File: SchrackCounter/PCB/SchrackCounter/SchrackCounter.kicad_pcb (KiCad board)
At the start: 2 copper layers, 38 parts, among them IC1 TPS565242DRLR, J1 TYPE-C-31-M-12, SW1 SW_DPDT_x2, SW2 SW_Push, SW3 SW_Push, SW4 SW_Push, SW5 SW_Push, U1 D168K, U2 DC56-11EWA, U3 D168K, U4 DC56-11EWA, U5 D168K, U7 ESP32-S3-WROOM-2, U8 USBLC6-2SC6

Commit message: sleep, overated imo
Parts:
- added BT1: Battery, Connector_Samtec_HPM_THT:Samtec_HPM-02-01-x-S_Straight_1x02_Pitch5.08mm, F.Cu at (144.7, 87.8)
- added BZ1: Buzzer, Schrack_brd:CUI_CPT-1625-80, F.Cu at (86.0, 102.3)
- added D2: LED, LED_SMD:LED_0805_2012Metric_Pad1.15x1.40mm_HandSolder, F.Cu at (76.4, 94.6)
- added D3: LED, LED_SMD:LED_0805_2012Metric_Pad1.15x1.40mm_HandSolder, F.Cu at (76.4, 97.6)
- added D4: LED, LED_SMD:LED_0805_2012Metric_Pad1.15x1.40mm_HandSolder, F.Cu at (76.4, 100.6)
- added D5: LED, LED_SMD:LED_0805_2012Metric_Pad1.15x1.40mm_HandSolder, F.Cu at (76.4, 103.7)
- added D6: LED, LED_SMD:LED_0805_2012Metric_Pad1.15x1.40mm_HandSolder, F.Cu at (76.4, 106.7)
- added D7: LED, LED_SMD:LED_0805_2012Metric_Pad1.15x1.40mm_HandSolder, F.Cu at (76.4, 109.8)
- added D8: LED, LED_SMD:LED_0805_2012Metric_Pad1.15x1.40mm_HandSolder, F.Cu at (76.4, 112.8)
- added D9: LED, LED_SMD:LED_0805_2012Metric_Pad1.15x1.40mm_HandSolder, F.Cu at (76.4, 115.8)
- added J2: Conn_01x02_Pin, Connector_PinHeader_2.54mm:PinHeader_1x02_P2.54mm_Vertical, F.Cu at (149.5, 65.5)
- added J3: Conn_01x02_Pin, Connector_JST:JST_XH_B2B-XH-A_1x02_P2.50mm_Vertical, F.Cu at (150.7, 58.7)
- added M1: Fan_CPU_4pin, Connector:FanPinHeader_1x04_P2.54mm_Vertical, F.Cu at (149.5, 51.0)
- added R10: 10k.mcu, Resistor_SMD:R_0805_2012Metric_Pad1.20x1.40mm_HandSolder, F.Cu at (149.6, 71.8)
- added R3: 10k, Resistor_SMD:R_0805_2012Metric_Pad1.20x1.40mm_HandSolder, F.Cu at (110.0, 81.6)
- added R7: 15R, Resistor_SMD:R_0805_2012Metric_Pad1.20x1.40mm_HandSolder, F.Cu at (95.7, 103.4)
- added R8: 220R, Resistor_SMD:R_0805_2012Metric_Pad1.20x1.40mm_HandSolder, F.Cu at (95.7, 106.3)
- added R9: 220R, Resistor_SMD:R_0805_2012Metric_Pad1.20x1.40mm_HandSolder, F.Cu at (95.7, 109.3)
- added SW6: SW_Push, Button_Switch_SMD:SW_SPST_EVQPE1, F.Cu at (142.7, 70.0)
- added SW7: SW_Push, Button_Switch_SMD:SW_SPST_EVQPE1, F.Cu at (142.7, 75.0)
- added SW8: SW_Push, Button_Switch_SMD:SW_SPST_EVQPE1, F.Cu at (142.7, 80.1)
- added TP3: TestPoint, Schrack_brd:SCHRACK_LOGO_IMG, F.Cu at (187.2, 77.2)
- added U6: MAX7219, Package_SO:SOIC-24W_7.5x15.4mm_P1.27mm, F.Cu at (101.2, 82.6)
- C10: value 100nF.mcu -> 100nF.max
- C9: value 10uF.mcu -> 10uF.max
- R4, R5: value 15R -> 220R
- R6: value 10k.mcu -> 15R
- moved TP1 180.2 mm to (224.2, 82.0)
- moved J1 113.3 mm to (84.8, 118.3)
- moved R4 108.4 mm to (95.7, 94.5)
- moved R5 108.4 mm to (95.7, 97.5)
- moved D1 103.6 mm to (97.4, 117.8)
- moved C13 97.8 mm to (100.4, 94.5)
- moved U8 95.9 mm to (97.8, 113.9)
- moved U1 94.0 mm to (76.8, 49.2), turned to 0 degrees
- moved R6 93.6 mm to (95.7, 100.4)
- moved TP2 89.5 mm to (183.9, 90.6)
- moved U3 89.3 mm to (76.8, 63.3), turned to 0 degrees
- moved U5 88.8 mm to (76.8, 77.3), turned to 0 degrees
- moved R1 75.8 mm to (136.0, 109.6)
- moved R2 75.8 mm to (136.0, 112.5)
- moved U2 74.5 mm to (97.6, 50.5), turned to 0 degrees
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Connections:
- net TEST PROGRAM 1 renamed DIGIT_SELECT
- net TEST PROGRAM 2 renamed TIME_UP
- R4 pad 1: D+ IN -> GREEN_FLASH
- R4 pad 2: Net-(R4-Pad2) -> Net-(D2-A)
- R5 pad 1: D- IN -> GREEN_FLASH
- R5 pad 2: Net-(R5-Pad2) -> Net-(D4-A)
- R6 pad 1: EN -> D+ IN
- R6 pad 2: +3V3 -> Net-(R6-Pad2)
- U7 pad 13: unconnected-(U7-IO19-Pad13) -> D-
- U7 pad 14: unconnected-(U7-IO20-Pad14) -> D+
- U7 pad 18: unconnected-(U7-IO10-Pad18) -> ~{CS}
- U7 pad 19: unconnected-(U7-IO11-Pad19) -> MOSI
- U7 pad 20: unconnected-(U7-IO12-Pad20) -> CLK
- U7 pad 36: unconnected-(U7-RXD0-Pad36) -> RX
- U7 pad 37: unconnected-(U7-TXD0-Pad37) -> TX
- U8 pad 1: Net-(R4-Pad2) -> Net-(R6-Pad2)
- U8 pad 3: Net-(R5-Pad2) -> Net-(R7-Pad2)

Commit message: pcb Update
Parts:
- removed U2, U4: DC56-11EWA, Display_7Segment:DA56-11SURKWA
- added U9: CA56-12SURKWA, Display_7Segment:CA56-12SURKWA, F.Cu at (197.2, 106.7)
- moved U6 135.7 mm to (233.8, 53.5), turned to 180 degrees
- moved U5 129.1 mm to (204.7, 59.0), turned to 90 degrees
- moved U3 114.6 mm to (191.4, 59.0), turned to 90 degrees
- moved C14 112.9 mm to (52.5, 113.5)
- moved C15 112.9 mm to (52.5, 116.5)
- moved TP1 104.4 mm to (265.8, -13.8)
- moved TP2 104.4 mm to (225.4, -5.19)
- moved TP3 104.4 mm to (228.8, -18.5)
- moved U1 101.8 mm to (178.2, 59.0), turned to 90 degrees
- moved U7 101.4 mm to (99.4, 9.45)
- moved R10 98.7 mm to (61.8, 116.8)
- moved C1 74.3 mm to (81.8, 144.8)
- moved C11 74.3 mm to (64.7, 132.6)
- moved C2 74.3 mm to (87.2, 144.7)
- moved C4 74.3 mm to (87.2, 147.8)
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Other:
- board outline added: 100 x 50 mm

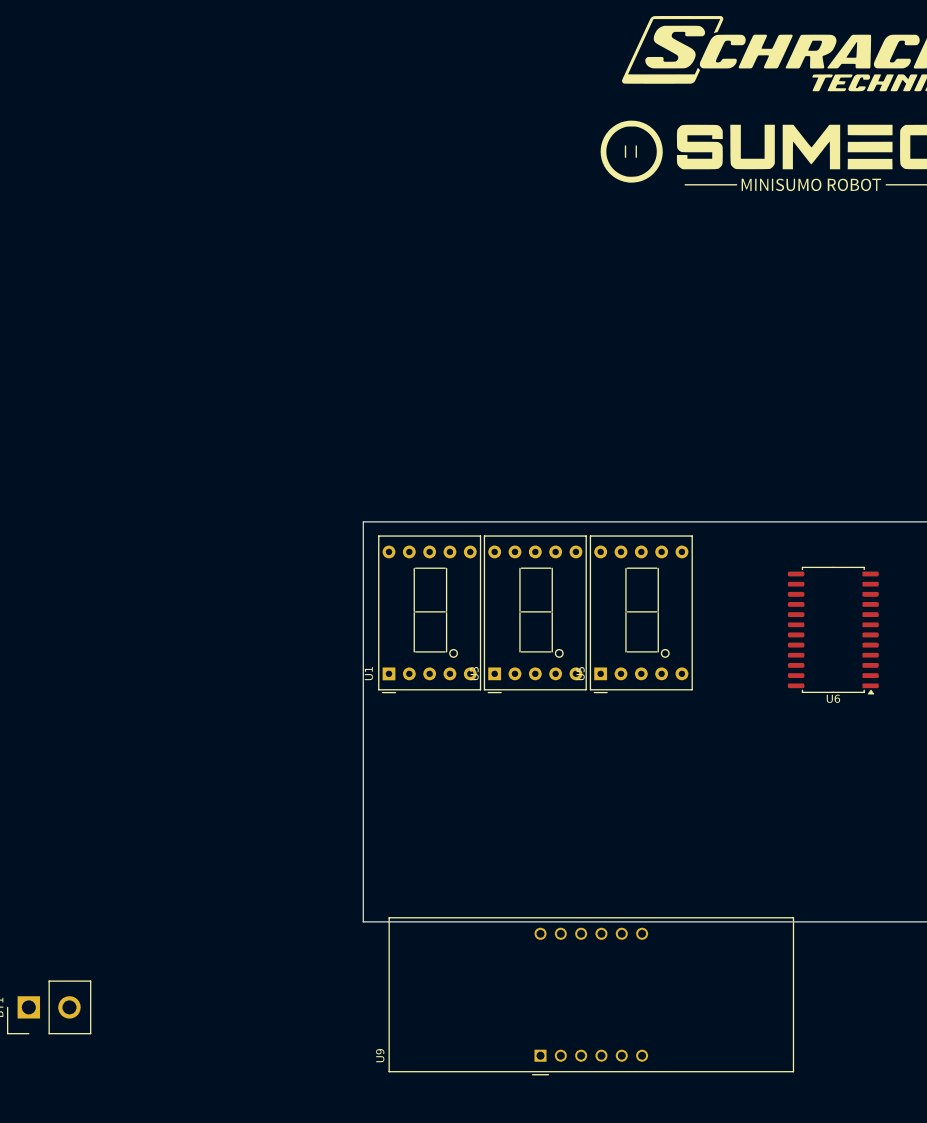
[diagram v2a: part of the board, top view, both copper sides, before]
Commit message: Custom symbol and footprints
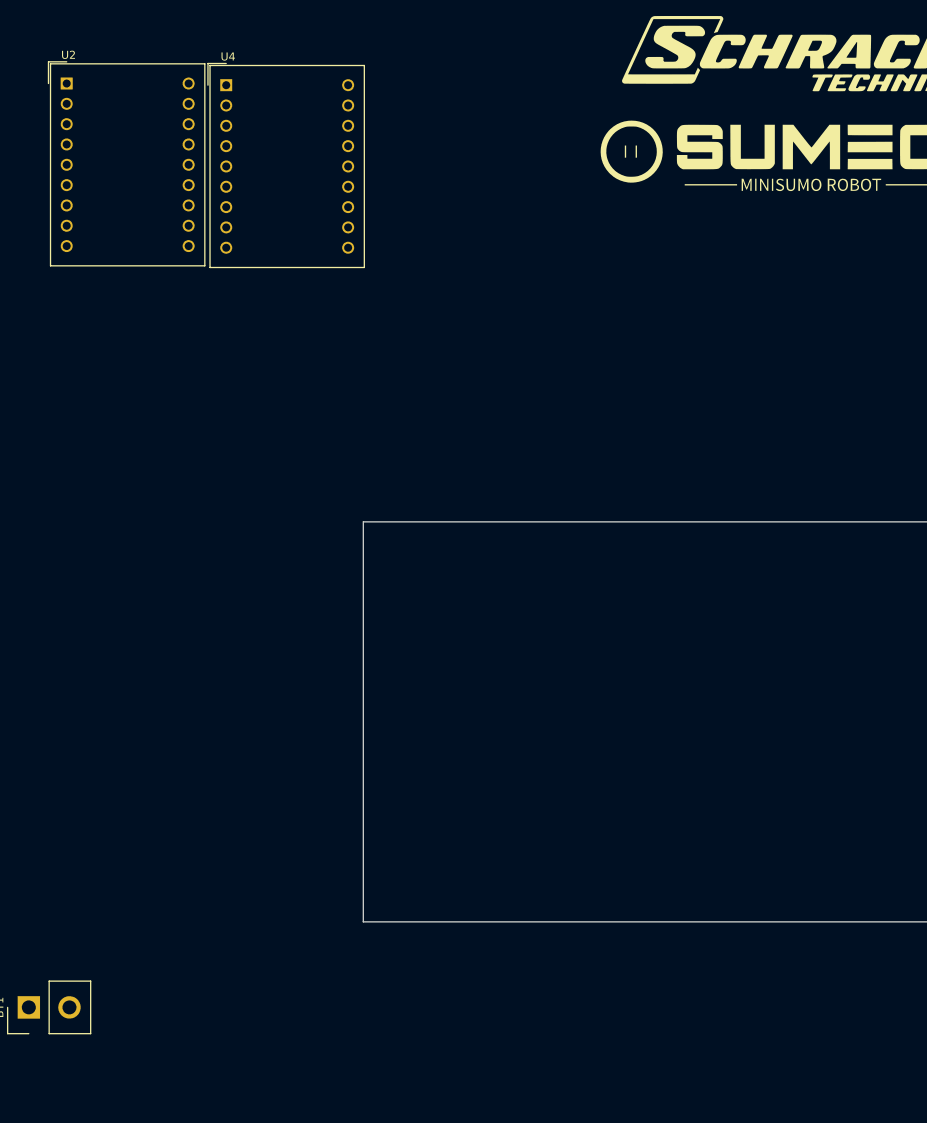
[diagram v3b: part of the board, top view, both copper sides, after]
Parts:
- removed U1, U3, U5: D168K, Display_7Segment:D1X8K
- removed U6: MAX7219, Package_SO:SOIC-24W_7.5x15.4mm_P1.27mm
- removed U9: CA56-12SURKWA, Display_7Segment:CA56-12SURKWA
- added U2: DC56-11EWA, Display_7Segment:DA56-11SURKWA, F.Cu at (137.9, -14.8)
- added U4: DC56-11EWA, Display_7Segment:DA56-11SURKWA, F.Cu at (157.9, -14.6)

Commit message: deletion of useless shit
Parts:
- added U1: LTD080BUE-103A, Schrack_brd:LTD080BUE-103A_made_by_bismarx, F.Cu at (178.8, 54.7)
- added U6: MAX7219, Package_SO:SOIC-24W_7.5x15.4mm_P1.27mm, F.Cu at (247.4, 56.2)
- moved U4 112.2 mm to (211.4, 84.0), turned to 90 degrees
- moved U2 109.8 mm to (185.7, 84.0), turned to 90 degrees
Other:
- board size 100 x 50 mm -> 100 x 65 mm

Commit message: new custom symbol + footprint, pcb layout
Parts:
- removed U4: DC56-11EWA, Display_7Segment:DA56-11SURKWA
- added U3: LTD080BUE-103A, Schrack_brd:LDD080BUE-101A_made_by_bismarx, F.Cu at (103.4, 70.9)
- U2: value DC56-11EWA -> LTD080BUE-103A; footprint Display_7Segment:DA56-11SURKWA -> Schrack_brd:LDD080BUE-101A_made_by_bismarx
- moved U6 278.5 mm to (-29.8, 28.5)
- moved TP1 244.7 mm to (23.2, -46.8)
- moved TP2 244.7 mm to (-17.1, -38.2)
- moved TP3 244.7 mm to (-13.8, -51.5)
- moved SW2 178.3 mm to (-92.5, 24.4)
- moved SW3 178.3 mm to (-92.5, 29.4)
- moved SW4 178.3 mm to (-92.5, 34.5)
- moved SW5 178.3 mm to (-92.5, 39.5)
- moved SW6 178.3 mm to (-92.5, 44.6)
- moved SW7 178.3 mm to (-92.5, 49.6)
- moved SW8 178.3 mm to (-92.5, 54.7)
- moved BZ1 164.5 mm to (-58.2, 45.5)
- moved C1 164.0 mm to (-81.7, 157.3)
- moved C10 164.0 mm to (-111.1, 99.3)
- moved C11 164.0 mm to (-98.8, 145.1)
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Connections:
- U2 pad 10: SEG_B -> SEG_F
- U2 pad 11: SEG_A -> SEG_G
- U2 pad 12: SEG_F -> SEG_B
- U2 pad 13: GND -> +3V3
- U2 pad 14: GND -> +3V3
- U2 pad 4: DP3 -> DP1
- U2 pad 5: SEG_E -> SEG_C
- U2 pad 7: SEG_G -> SEG_A
- U2 pad 8: SEG_C -> SEG_E
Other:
- copper layers 2 -> 4
- board text added: "BUTTONS"
- board text added: "Who and how will make holes for the Schrack buttons, Dimensions needed: - Schrack tactile switches - Schrack light switch (the main premise)"

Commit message: Im doing 3d models now i guess
New 3digit and 2digit 3d models, kinda proud of them even tho im committed 5 warcrimes while making them
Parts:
- moved U2 1.22 mm to (65.7, 70.2)
- moved U1 0.90 mm to (68.0, 105.2)
- moved U3 0.86 mm to (103.0, 70.2)

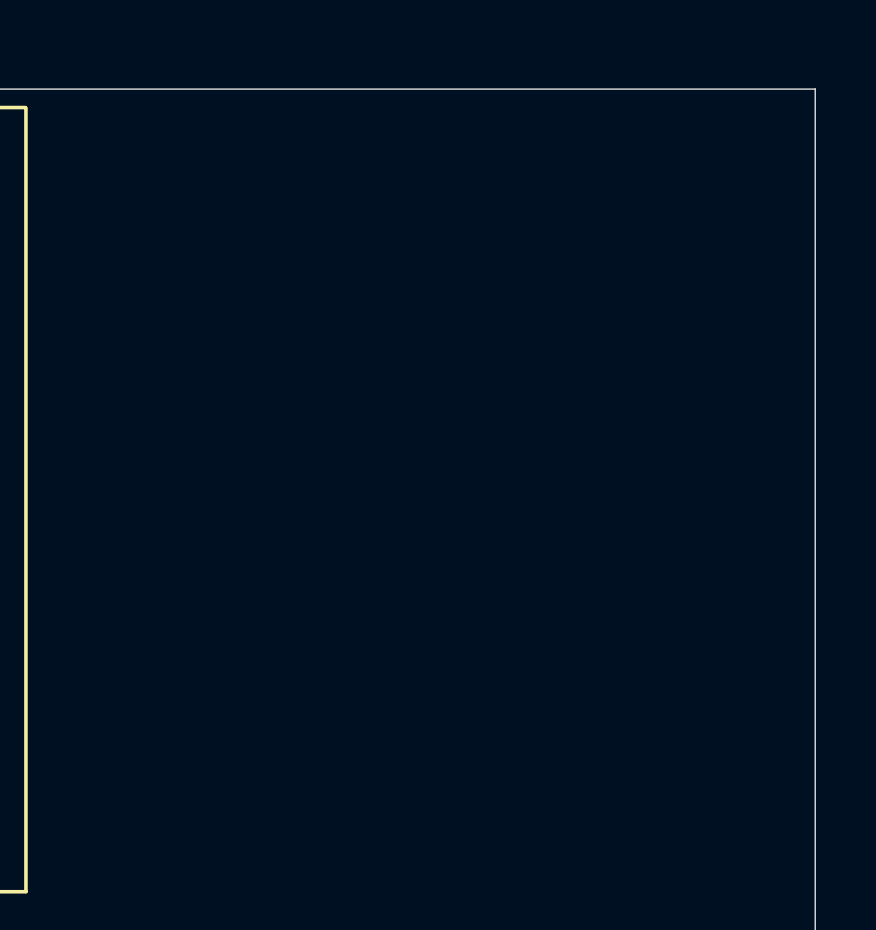
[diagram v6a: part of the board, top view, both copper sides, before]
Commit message: libs cleanup, sd card added
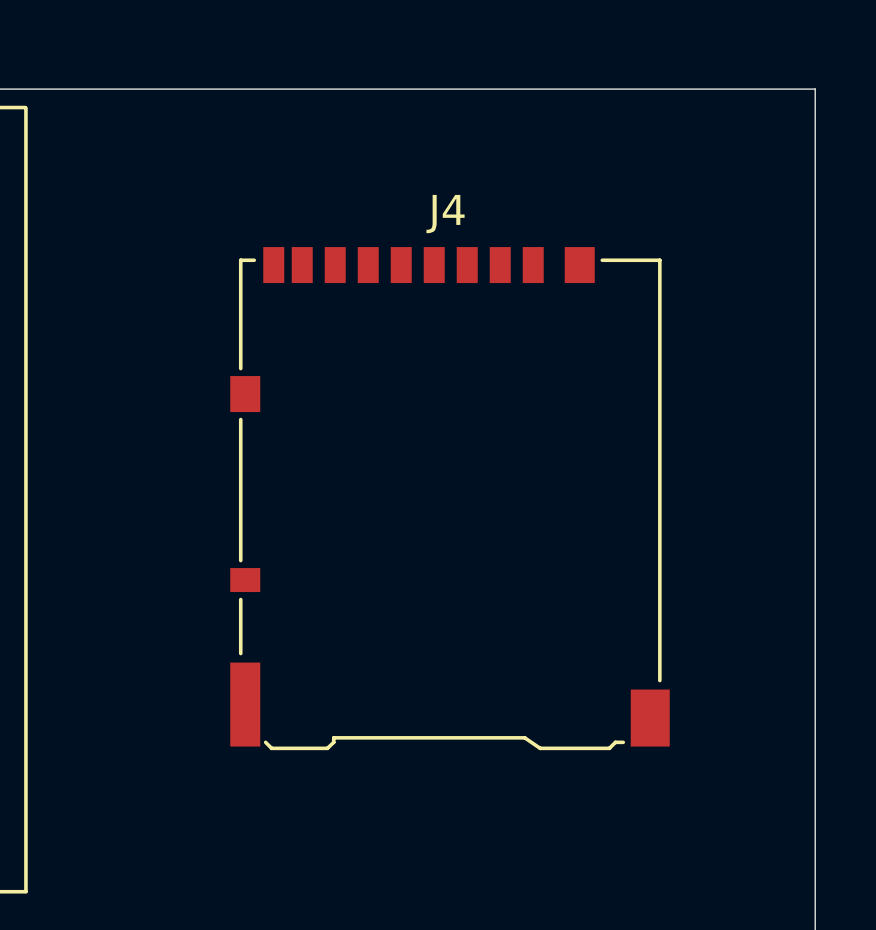
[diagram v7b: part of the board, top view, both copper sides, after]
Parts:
- added J4: Micro_SD_Card_Det_Hirose_DM3AT, Connector_Card:microSD_HC_Hirose_DM3AT-SF-PEJM5, F.Cu at (153.1, 57.1)

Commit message: SD card addition
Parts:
- removed U6: MAX7219, Package_SO:SOIC-24W_7.5x15.4mm_P1.27mm
- J4: value Micro_SD_Card_Det_Hirose_DM3AT -> MEM2067-02-180-00-A_REVB; footprint Connector_Card:microSD_HC_Hirose_DM3AT-SF-PEJM5 -> Schrack_brd:GCT_MEM2067-02-180-00-A_REVB
- U1: value LTD080BUE-103A -> LDD080BUE-101A; footprint Schrack_brd:LTD080BUE-103A_made_by_bismarx -> Schrack_brd:LDD080BUE-101A_made_by_bismarx
- U2: footprint Schrack_brd:LDD080BUE-101A_made_by_bismarx -> Schrack_brd:LTD080BUE-103A_made_by_bismarx
- U3: value LTD080BUE-103A -> LDD080BUE-101A
- moved U7 222.8 mm to (155.6, 58.9), turned to -90 degrees
- moved SW2 143.2 mm to (-36.0, 155.9), turned to 90 degrees
- moved SW3 140.7 mm to (-30.9, 155.9), turned to 90 degrees
- moved SW4 138.5 mm to (-25.9, 155.9), turned to 90 degrees
- moved SW5 136.7 mm to (-20.8, 155.9), turned to 90 degrees
- moved SW6 135.2 mm to (-15.8, 155.9), turned to 90 degrees
- moved SW7 134.1 mm to (-10.7, 155.9), turned to 90 degrees
- moved SW8 133.4 mm to (-5.65, 155.9), turned to 90 degrees
- moved C15 105.7 mm to (-5.99, 141.2), turned to 90 degrees
- moved C14 103.1 mm to (-9.00, 141.2), turned to 90 degrees
- moved R9 99.0 mm to (-15.1, 141.8), turned to 90 degrees
- moved R8 96.8 mm to (-18.0, 141.8), turned to 90 degrees
- moved R10 96.0 mm to (-5.75, 132.0), turned to 90 degrees
- moved R2 95.6 mm to (-8.50, 115.4), turned to 90 degrees
- moved R7 94.8 mm to (-21.0, 141.8), turned to 90 degrees
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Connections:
- J4 pad 10: unconnected-(J4-DET_A-Pad10) -> Net-(J4-SHIELD-Pad10)
- J4 pad 11: unconnected-(J4-SHIELD-Pad11) -> Net-(J4-SHIELD-Pad10)
- J4 pad 9: unconnected-(J4-DET_B-Pad9) -> Net-(J4-SHIELD-Pad10)
- U1 pad 1: +3V3 -> SEG_E
- U1 pad 10: +3V3 -> SEG_F
- U1 pad 11: SEG_A -> SEG_G
- U1 pad 2: SEG_C -> SEG_D
- U1 pad 3: +3V3 -> SEG_C
- U1 pad 4: SEG_B -> DP1
- U1 pad 5: SEG_D -> SEG_C
- U1 pad 6: DPX -> SEG_D
- U1 pad 7: SEG_E -> SEG_A
- U1 pad 8: SEG_F -> SEG_E
- U1 pad 9: SEG_G -> DP2
- U2 pad 1: SEG_E -> +3V3
- U2 pad 10: SEG_F -> +3V3
- U2 pad 11: SEG_G -> SEG_A
- U2 pad 2: SEG_D -> SEG_C
- U2 pad 3: SEG_C -> +3V3
- U2 pad 4: DP1 -> SEG_B
- U2 pad 5: SEG_C -> SEG_D
- U2 pad 6: SEG_D -> DPX
- U2 pad 7: SEG_A -> SEG_E
- U2 pad 8: SEG_E -> SEG_F
- U2 pad 9: DP2 -> SEG_G
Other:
- board size 100 x 65 mm -> 335.5 x 113.7 mm
